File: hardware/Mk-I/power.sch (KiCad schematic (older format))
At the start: 12 parts, among them CON1 USB-MICRO-B, U2 MCP73831, U3 BD33IA5

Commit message: HW: Add a DFU mode switch
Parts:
- C1, C2, C3: symbol C -> C-RESCUE-wnm_mk_1
- R1, R2: symbol R -> R-RESCUE-wnm_mk_1
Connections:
- wire segments 26 -> 28
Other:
- moved on the sheet: BAT1
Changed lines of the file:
@@
 EESchema Schematic File Version 2
+LIBS:wnm_mk_1-rescue
 LIBS:power
 LIBS:device
@@
 LIBS:microchip_pic12mcu
 LIBS:microchip_pic16mcu
-LIBS:microchip1
 LIBS:msp430
 LIBS:nxp_armmcu
@@
 LIBS:relays
 LIBS:sensors
-LIBS:special
 LIBS:stm8
 LIBS:stm32
@@
 $EndComp
 $Comp
-L GND #PWR07
+L GND-RESCUE-wnm_mk_1 #PWR07
 U 1 1 585D2F29
 P 4400 2900
+AR Path="/585D2F29" Ref="#PWR07"  Part="1"
+AR Path="/585D2CBE/585D2F29" Ref="#PWR07"  Part="1"
 F 0 "#PWR07" H 4400 2900 30  0001 C CNN
 F 1 "GND" H 4400 2830 30  0001 C CNN
@@
 	3750 2700 4700 2700
 $Comp
-L R R2
+L R-RESCUE-wnm_mk_1 R2
 U 1 1 585D2F62
 P 4050 2500
+AR Path="/585D2F62" Ref="R2"  Part="1"
+AR Path="/585D2CBE/585D2F62" Ref="R2"  Part="1"
 F 0 "R2" V 4130 2500 40  0000 C CNN
 F 1 "10K" V 4057 2501 40  0000 C CNN
@@
 Connection ~ 4400 2700
 $Comp
-L C C1
+L C-RESCUE-wnm_mk_1 C1
 U 1 1 585D3088
 P 4700 2500
+AR Path="/585D3088" Ref="C1"  Part="1"
+AR Path="/585D2CBE/585D3088" Ref="C1"  Part="1"
 F 0 "C1" H 4700 2600 40  0000 L CNN
 F 1 "10uF" H 4706 2415 40  0000 L CNN
@@
 U 1 1 585D348C
 P 1950 2700
+AR Path="/585D348C" Ref="BAT1"  Part="1"
+AR Path="/585D2CBE/585D348C" Ref="BAT1"  Part="1"
 F 0 "BAT1" H 1950 2800 50  0000 C CNN
 F 1 "LED" H 1950 2600 50  0000 C CNN
@@
 F 3 "" H 1950 2700 60  0000 C CNN
 	1    1950 2700
-	1    0    0    -1
-$EndComp
-$Comp
-L R R1
+	-1   0    0    1
+$EndComp
+$Comp
+L R-RESCUE-wnm_mk_1 R1
 U 1 1 585D34C3
 P 2400 2700
+AR Path="/585D34C3" Ref="R1"  Part="1"
+AR Path="/585D2CBE/585D34C3" Ref="R1"  Part="1"
 F 0 "R1" V 2480 2700 40  0000 C CNN
 F 1 "1K" V 2407 2701 40  0000 C CNN
@@
 VIN
 $Comp
-L GND #PWR010
+L GND-RESCUE-wnm_mk_1 #PWR010
 U 1 1 585D49CE
 P 7750 2500
+AR Path="/585D49CE" Ref="#PWR010"  Part="1"
+AR Path="/585D2CBE/585D49CE" Ref="#PWR010"  Part="1"
 F 0 "#PWR010" H 7750 2500 30  0001 C CNN
 F 1 "GND" H 7750 2430 30  0001 C CNN
@@
 VIN
 $Comp
-L C C3
+L C-RESCUE-wnm_mk_1 C3
 U 1 1 585D5B09
 P 9600 2100
+AR Path="/585D5B09" Ref="C3"  Part="1"
+AR Path="/585D2CBE/585D5B09" Ref="C3"  Part="1"
 F 0 "C3" H 9600 2200 40  0000 L CNN
 F 1 "47uF" H 9606 2015 40  0000 L CNN
@@
 $EndComp
 $Comp
-L GND #PWR012
+L GND-RESCUE-wnm_mk_1 #PWR012
 U 1 1 585D5C16
 P 9600 2300
+AR Path="/585D5C16" Ref="#PWR012"  Part="1"
+AR Path="/585D2CBE/585D5C16" Ref="#PWR012"  Part="1"
 F 0 "#PWR012" H 9600 2300 30  0001 C CNN
 F 1 "GND" H 9600 2230 30  0001 C CNN
@@
 $EndComp
 $Comp
-L C C2
+L C-RESCUE-wnm_mk_1 C2
 U 1 1 585D5D4C
 P 7750 2100
+AR Path="/585D5D4C" Ref="C2"  Part="1"
+AR Path="/585D2CBE/585D5D4C" Ref="C2"  Part="1"
 F 0 "C2" H 7750 2200 40  0000 L CNN
 F 1 "4.7uF" H 7756 2015 40  0000 L CNN
@@
 Connection ~ 5200 4800
 $Comp
-L GND #PWR013
+L GND-RESCUE-wnm_mk_1 #PWR013
 U 1 1 585CFC1E
 P 5200 5000
+AR Path="/585CFC1E" Ref="#PWR013"  Part="1"
+AR Path="/585D2CBE/585CFC1E" Ref="#PWR013"  Part="1"
 F 0 "#PWR013" H 5200 5000 30  0001 C CNN
 F 1 "GND" H 5200 4930 30  0001 C CNN
@@
 	3700 4800 3700 5000
 $Comp
-L GND #PWR014
+L GND-RESCUE-wnm_mk_1 #PWR014
 U 1 1 585CFC9F
 P 3700 5000
+AR Path="/585CFC9F" Ref="#PWR014"  Part="1"
+AR Path="/585D2CBE/585CFC9F" Ref="#PWR014"  Part="1"
 F 0 "#PWR014" H 3700 5000 30  0001 C CNN
 F 1 "GND" H 3700 4930 30  0001 C CNN
@@
 VBAT
 $Comp
-L GND #PWR015
+L GND-RESCUE-wnm_mk_1 #PWR015
 U 1 1 585D1BAC
 P 2150 4800
+AR Path="/585D1BAC" Ref="#PWR015"  Part="1"
+AR Path="/585D2CBE/585D1BAC" Ref="#PWR015"  Part="1"
 F 0 "#PWR015" H 2150 4800 30  0001 C CNN
 F 1 "GND" H 2150 4730 30  0001 C CNN
@@
 	1    0    0    -1
 $EndComp
+Wire Wire Line
+	1800 2700 1750 2700
+Wire Wire Line
+	2100 2700 2150 2700
 $EndSCHEMATC

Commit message: HW: Fix regulator footprint
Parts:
- U3: footprint Housings_SSOP:MSOP-8-1EP_3x3mm_Pitch0.65mm -> POSS:HTSOP-J8
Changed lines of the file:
@@
 F 0 "U3" H 8400 1650 60  0000 C CNN
 F 1 "BD33IA5" H 8650 1500 60  0000 C CNN
-F 2 "Housings_SSOP:MSOP-8-1EP_3x3mm_Pitch0.65mm" H 8650 1500 60  0001 C CNN
+F 2 "POSS:HTSOP-J8" H 8650 1500 60  0001 C CNN
 F 3 "" H 8650 1500 60  0001 C CNN
 	1    8650 1500

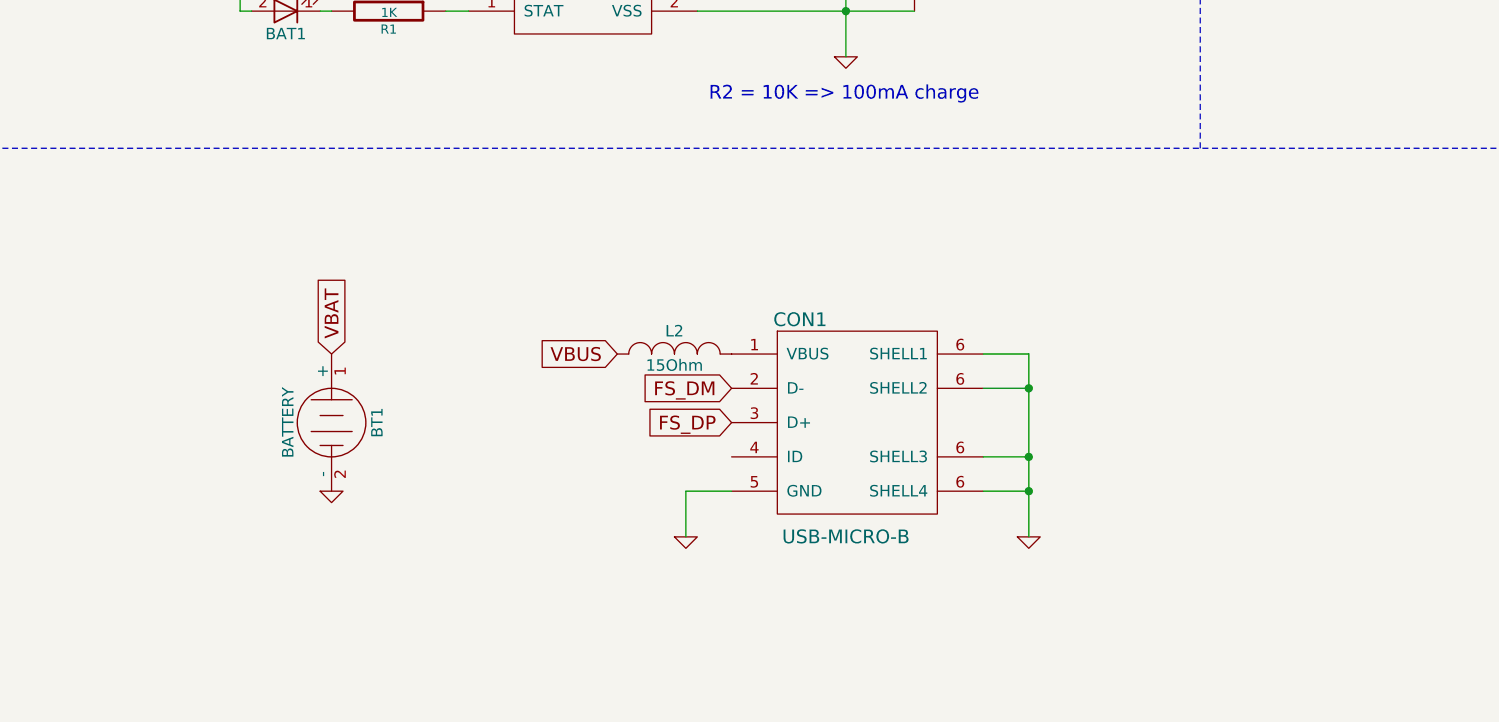
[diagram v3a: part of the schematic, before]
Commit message: HW: Divide VBAT before connecting to the MCU
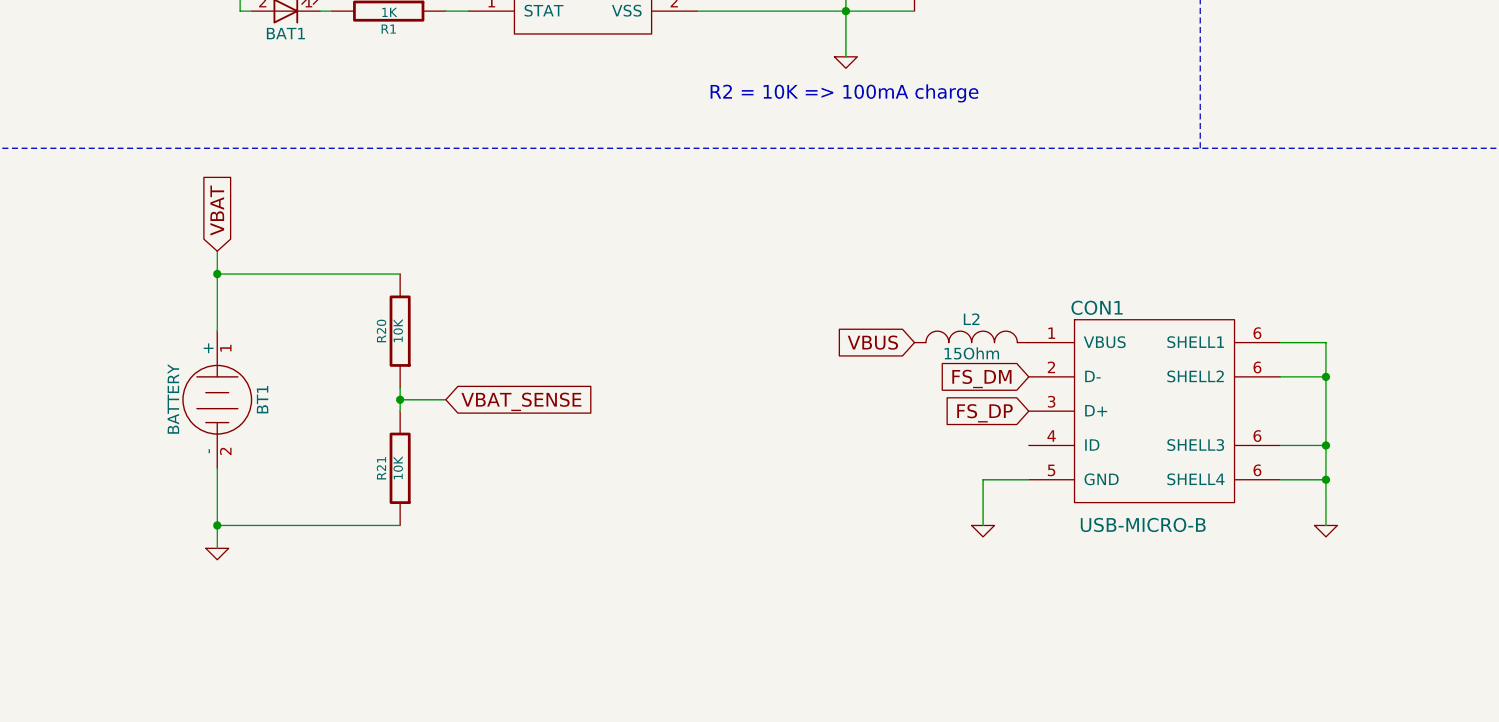
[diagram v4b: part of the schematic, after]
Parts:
- added R20, R21: 10K, Resistors_SMD:R_0805, symbol R-RESCUE-wnm_mk_1
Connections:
- net GND: now also R21.1
- net VBAT: now also R20.2
- new net VBAT_SENSE: R20.1, R21.2
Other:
- moved on the sheet: BT1, CON1, L2
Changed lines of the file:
@@
 L USB-MICRO-B CON1
 U 1 1 585CF6A2
-P 4450 4500
-F 0 "CON1" H 4200 4950 60  0000 C CNN
-F 1 "USB-MICRO-B" H 4400 4000 60  0000 C CNN
-F 2 "Connect:USB_Micro-B" H 4450 4500 60  0001 C CNN
-F 3 "" H 4450 4500 60  0001 C CNN
-	1    4450 4500
+P 5750 4450
+F 0 "CON1" H 5500 4900 60  0000 C CNN
+F 1 "USB-MICRO-B" H 5700 3950 60  0000 C CNN
+F 2 "Connect:USB_Micro-B" H 5750 4450 60  0001 C CNN
+F 3 "" H 5750 4450 60  0001 C CNN
+	1    5750 4450
 	1    0    0    -1
 $EndComp
 Wire Wire Line
-	5000 4200 5200 4200
+	6300 4150 6500 4150
 Wire Wire Line
-	5200 4200 5200 5000
+	6500 4150 6500 4950
 Wire Wire Line
-	5000 4350 5200 4350
-Connection ~ 5200 4350
+	6300 4300 6500 4300
+Connection ~ 6500 4300
 Wire Wire Line
-	5000 4650 5200 4650
-Connection ~ 5200 4650
+	6300 4600 6500 4600
+Connection ~ 6500 4600
 Wire Wire Line
-	5000 4800 5200 4800
-Connection ~ 5200 4800
+	6300 4750 6500 4750
+Connection ~ 6500 4750
 $Comp
 L GND-RESCUE-wnm_mk_1 #PWR013
 U 1 1 585CFC1E
-P 5200 5000
+P 6500 4950
 AR Path="/585CFC1E" Ref="#PWR013"  Part="1"
 AR Path="/585D2CBE/585CFC1E" Ref="#PWR013"  Part="1"
-F 0 "#PWR013" H 5200 5000 30  0001 C CNN
-F 1 "GND" H 5200 4930 30  0001 C CNN
-F 2 "" H 5200 5000 60  0001 C CNN
-F 3 "" H 5200 5000 60  0001 C CNN
-	1    5200 5000
+F 0 "#PWR013" H 6500 4950 30  0001 C CNN
+F 1 "GND" H 6500 4880 30  0001 C CNN
+F 2 "" H 6500 4950 60  0001 C CNN
+F 3 "" H 6500 4950 60  0001 C CNN
+	1    6500 4950
 	1    0    0    -1
 $EndComp
-Text GLabel 3400 4200 0    60   Input ~ 0
+Text GLabel 4700 4150 0    60   Input ~ 0
 VBUS
 Wire Wire Line
-	3900 4800 3700 4800
+	5200 4750 5000 4750
 Wire Wire Line
-	3700 4800 3700 5000
+	5000 4750 5000 4950
 $Comp
 L GND-RESCUE-wnm_mk_1 #PWR014
 U 1 1 585CFC9F
-P 3700 5000
+P 5000 4950
 AR Path="/585CFC9F" Ref="#PWR014"  Part="1"
 AR Path="/585D2CBE/585CFC9F" Ref="#PWR014"  Part="1"
-F 0 "#PWR014" H 3700 5000 30  0001 C CNN
-F 1 "GND" H 3700 4930 30  0001 C CNN
-F 2 "" H 3700 5000 60  0001 C CNN
-F 3 "" H 3700 5000 60  0001 C CNN
-	1    3700 5000
+F 0 "#PWR014" H 5000 4950 30  0001 C CNN
+F 1 "GND" H 5000 4880 30  0001 C CNN
+F 2 "" H 5000 4950 60  0001 C CNN
+F 3 "" H 5000 4950 60  0001 C CNN
+	1    5000 4950
 	1    0    0    -1
 $EndComp
@@
 	-1   0    0    1
 $EndComp
-Text GLabel 3900 4350 0    60   Input ~ 0
+Text GLabel 5200 4300 0    60   Input ~ 0
 FS_DM
-Text GLabel 3900 4500 0    60   Input ~ 0
+Text GLabel 5200 4450 0    60   Input ~ 0
 FS_DP
 $Comp
 L BATTERY BT1
 U 1 1 585D1A2B
-P 2150 4500
-F 0 "BT1" H 2150 4700 50  0000 C CNN
-F 1 "BATTERY" H 2150 4310 50  0000 C CNN
-F 2 "Connect:PINHEAD1-2" H 2150 4500 60  0001 C CNN
-F 3 "" H 2150 4500 60  0000 C CNN
-	1    2150 4500
+P 1650 4400
+F 0 "BT1" H 1650 4600 50  0000 C CNN
+F 1 "BATTERY" H 1650 4210 50  0000 C CNN
+F 2 "Connect:PINHEAD1-2" H 1650 4400 60  0001 C CNN
+F 3 "" H 1650 4400 60  0000 C CNN
+	1    1650 4400
 	0    1    1    0
 $EndComp
-Text GLabel 2150 4200 1    60   Input ~ 0
+Text GLabel 1650 3750 1    60   Input ~ 0
 VBAT
 $Comp
 L GND-RESCUE-wnm_mk_1 #PWR015
 U 1 1 585D1BAC
-P 2150 4800
+P 1650 5050
 AR Path="/585D1BAC" Ref="#PWR015"  Part="1"
 AR Path="/585D2CBE/585D1BAC" Ref="#PWR015"  Part="1"
-F 0 "#PWR015" H 2150 4800 30  0001 C CNN
-F 1 "GND" H 2150 4730 30  0001 C CNN
-F 2 "" H 2150 4800 60  0001 C CNN
-F 3 "" H 2150 4800 60  0001 C CNN
-	1    2150 4800
+F 0 "#PWR015" H 1650 5050 30  0001 C CNN
+F 1 "GND" H 1650 4980 30  0001 C CNN
+F 2 "" H 1650 5050 60  0001 C CNN
+F 3 "" H 1650 5050 60  0001 C CNN
+	1    1650 5050
 	1    0    0    -1
 $EndComp
@@
 L INDUCTOR_SMALL L2
 U 1 1 58628564
-P 3650 4200
-F 0 "L2" H 3650 4300 50  0000 C CNN
-F 1 "15Ohm" H 3650 4150 50  0000 C CNN
-F 2 "Capacitors_SMD:C_0805" H 3650 4200 60  0001 C CNN
-F 3 "" H 3650 4200 60  0000 C CNN
-	1    3650 4200
+P 4950 4150
+F 0 "L2" H 4950 4250 50  0000 C CNN
+F 1 "15Ohm" H 4950 4100 50  0000 C CNN
+F 2 "Capacitors_SMD:C_0805" H 4950 4150 60  0001 C CNN
+F 3 "" H 4950 4150 60  0000 C CNN
+	1    4950 4150
 	1    0    0    -1
 $EndComp
@@
 Wire Wire Line
 	2100 2700 2150 2700
+$Comp
+L R-RESCUE-wnm_mk_1 R20
+U 1 1 58C51D7C
+P 2450 4100
+F 0 "R20" V 2530 4100 40  0000 C CNN
+F 1 "10K" V 2457 4101 40  0000 C CNN
+F 2 "Resistors_SMD:R_0805" V 2380 4100 30  0001 C CNN
+F 3 "" H 2450 4100 30  0000 C CNN
+	1    2450 4100
+	-1   0    0    1
+$EndComp
+$Comp
+L R-RESCUE-wnm_mk_1 R21
+U 1 1 58C51E89
+P 2450 4700
+F 0 "R21" V 2530 4700 40  0000 C CNN
+F 1 "10K" V 2457 4701 40  0000 C CNN
+F 2 "Resistors_SMD:R_0805" V 2380 4700 30  0001 C CNN
+F 3 "" H 2450 4700 30  0000 C CNN
+	1    2450 4700
+	-1   0    0    1
+$EndComp
+Wire Wire Line
+	2450 4350 2450 4450
+Wire Wire Line
+	2450 3850 1650 3850
+Wire Wire Line
+	1650 3750 1650 4100
+Wire Wire Line
+	1650 4700 1650 5050
+Wire Wire Line
+	1650 4950 2450 4950
+Connection ~ 1650 4950
+Connection ~ 1650 3850
+Wire Wire Line
+	2450 4400 2650 4400
+Connection ~ 2450 4400
+Text GLabel 2650 4400 2    60   Input ~ 0
+VBAT_SENSE
 $EndSCHEMATC

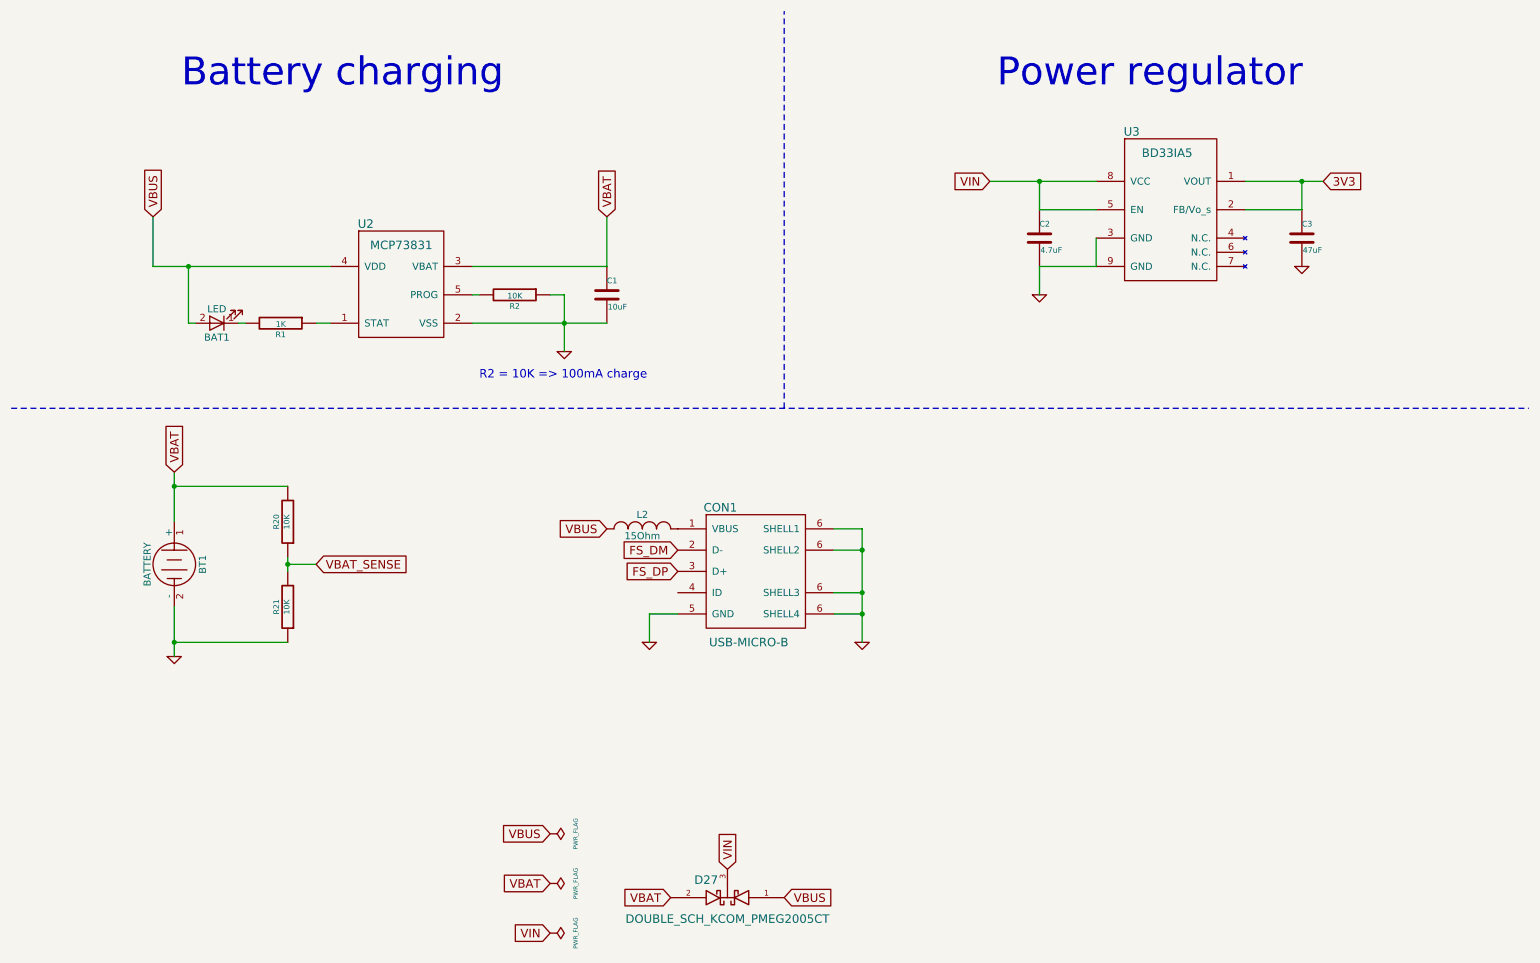
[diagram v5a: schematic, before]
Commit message: HW: Update parts value
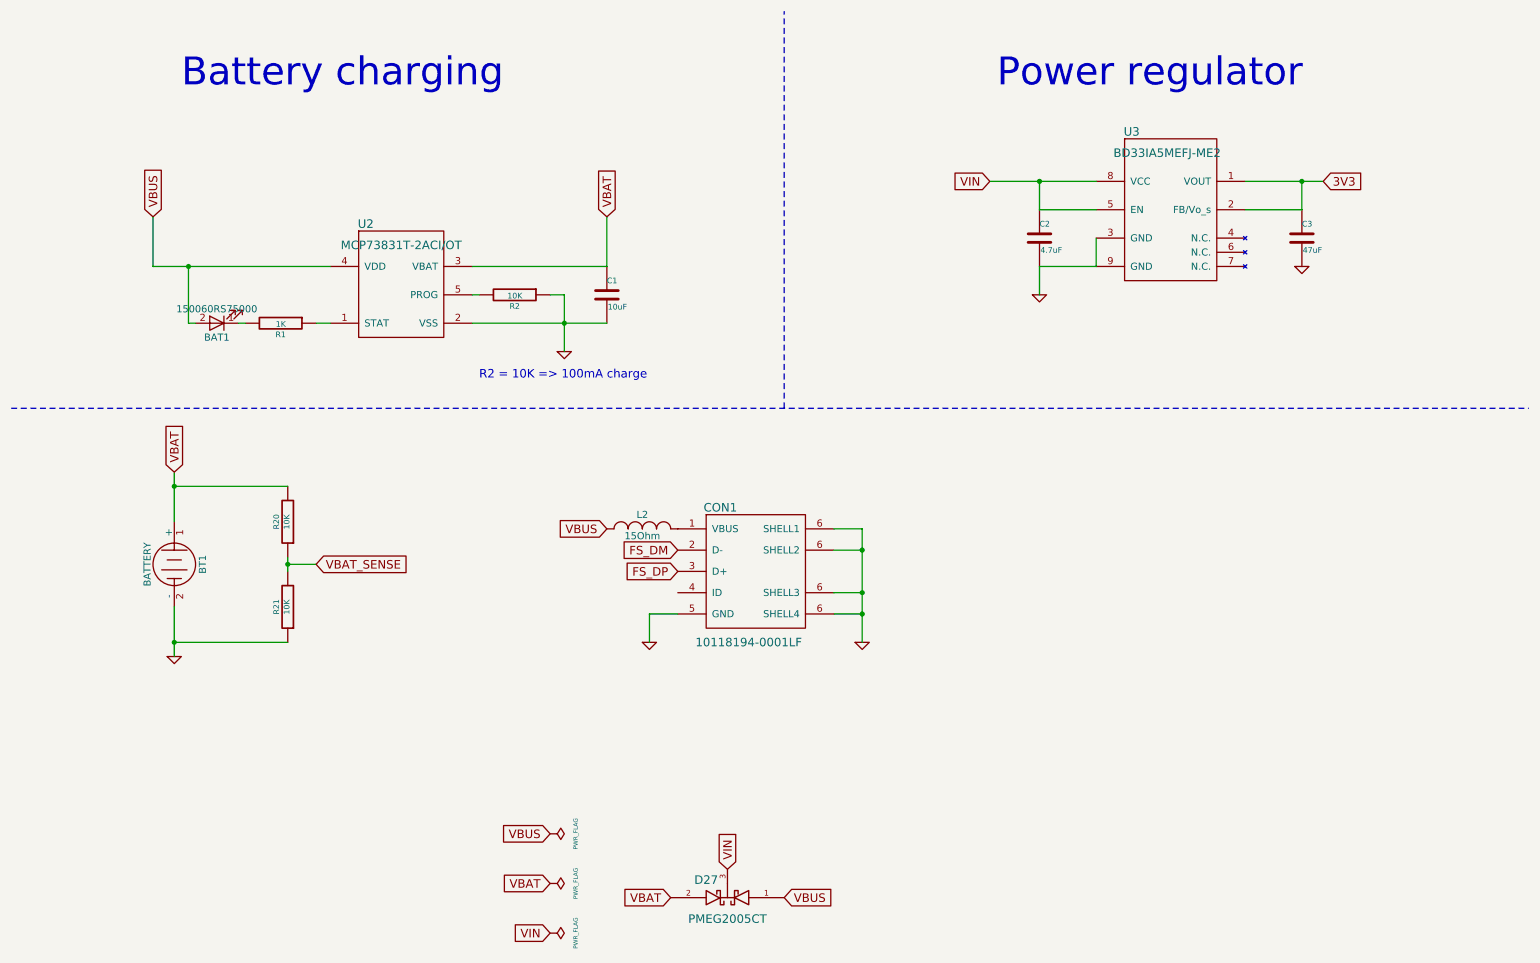
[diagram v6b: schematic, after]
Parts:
- BAT1: value LED -> 150060RS75000
- CON1: value USB-MICRO-B -> 10118194-0001LF
- D27: value DOUBLE_SCH_KCOM_PMEG2005CT -> PMEG2005CT
- U2: value MCP73831 -> MCP73831T-2ACI/OT
- U3: value BD33IA5 -> BD33IA5MEFJ-ME2
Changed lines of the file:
@@
 P 3250 2400
 F 0 "U2" H 3000 2800 60  0000 C CNN
-F 1 "MCP73831" H 3250 2650 60  0000 C CNN
+F 1 "MCP73831T-2ACI/OT" H 3250 2650 60  0000 C CNN
 F 2 "TO_SOT_Packages_SMD:SOT-23-5" H 3000 2850 60  0001 C CNN
 F 3 "" H 3000 2850 60  0001 C CNN
@@
 AR Path="/585D2CBE/585D348C" Ref="BAT1"  Part="1"
 F 0 "BAT1" H 1950 2800 50  0000 C CNN
-F 1 "LED" H 1950 2600 50  0000 C CNN
+F 1 "150060RS75000" H 1950 2600 50  0000 C CNN
 F 2 "LEDs:LED_0805" H 1950 2700 60  0001 C CNN
 F 3 "" H 1950 2700 60  0000 C CNN
@@
 P 8650 1500
 F 0 "U3" H 8400 1650 60  0000 C CNN
-F 1 "BD33IA5" H 8650 1500 60  0000 C CNN
+F 1 "BD33IA5MEFJ-ME2" H 8650 1500 60  0000 C CNN
 F 2 "POSS:HTSOP-J8" H 8650 1500 60  0001 C CNN
 F 3 "" H 8650 1500 60  0001 C CNN
@@
 P 5750 4450
 F 0 "CON1" H 5500 4900 60  0000 C CNN
-F 1 "USB-MICRO-B" H 5700 3950 60  0000 C CNN
+F 1 "10118194-0001LF" H 5700 3950 60  0000 C CNN
 F 2 "Connect:USB_Micro-B" H 5750 4450 60  0001 C CNN
 F 3 "" H 5750 4450 60  0001 C CNN
@@
 P 5550 6750
 F 0 "D27" H 5700 6625 60  0000 C CNN
-F 1 "DOUBLE_SCH_KCOM_PMEG2005CT" H 5550 6900 60  0000 C CNN
+F 1 "PMEG2005CT" H 5550 6900 60  0000 C CNN
 F 2 "TO_SOT_Packages_SMD:SOT-23" H 5550 6750 60  0001 C CNN
 F 3 "" H 5550 6750 60  0000 C CNN
